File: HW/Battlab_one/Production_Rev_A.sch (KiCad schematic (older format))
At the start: 51 parts, among them IC2 MIC5225-5.0YM5-TR, J1 BANANA_CONN, J3 BANANA_CONN, P1 USB_C_Plug, T1 750315371

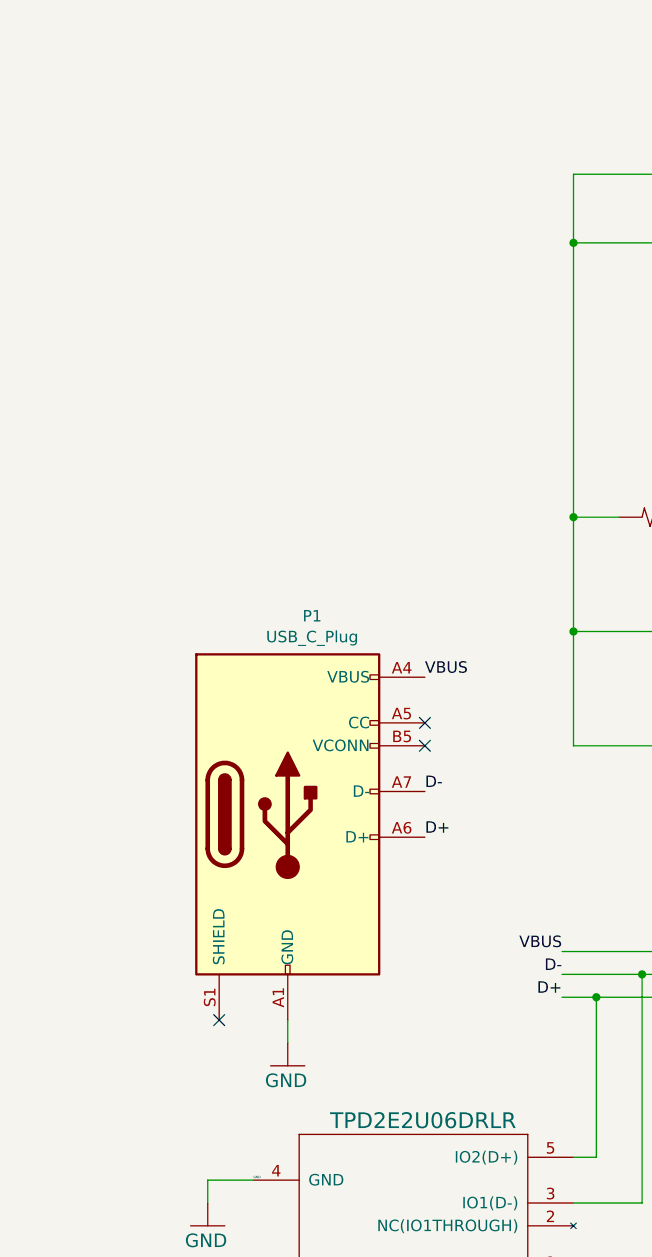
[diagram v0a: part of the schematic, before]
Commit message: USB-C resistor
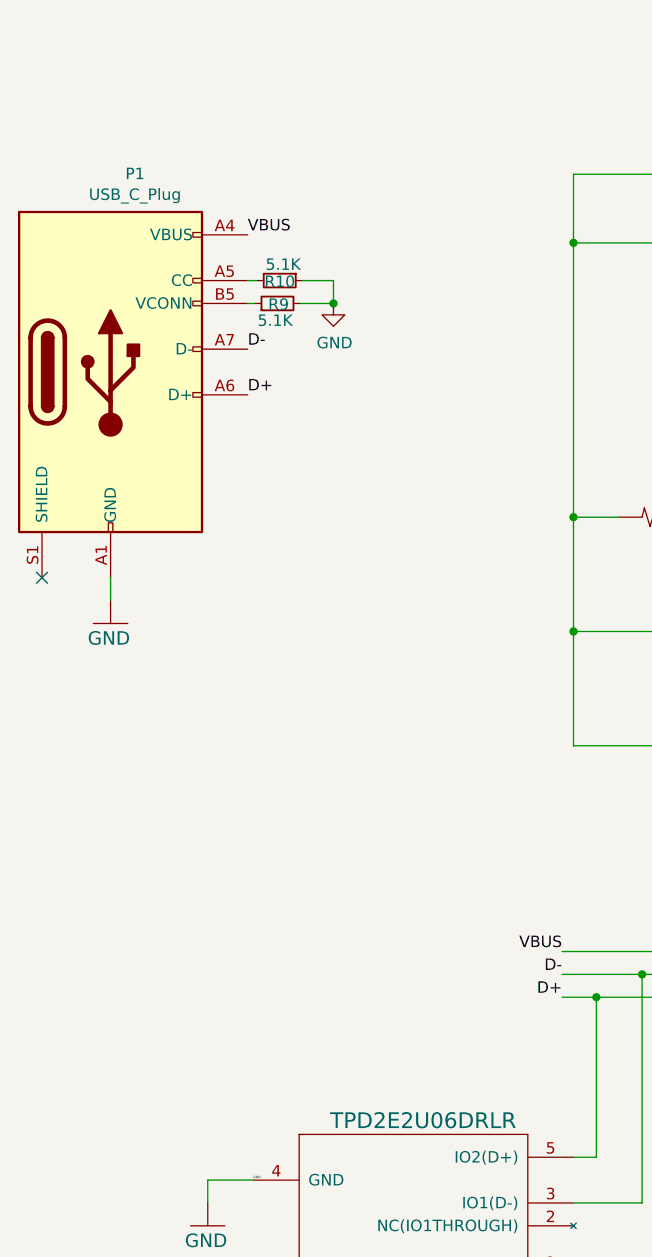
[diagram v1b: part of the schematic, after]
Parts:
- added R10, R9: 5.1K, Resistor_SMD:R_0805_2012Metric, symbol Device:R_Small
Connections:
- net GND: now also R10.1, R9.2
- net at P1.A5 (CC): now also R10.2
- net at P1.B5 (VCONN): now also R9.1
- no-connect marks 3 -> 1
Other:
- moved on the sheet: P1
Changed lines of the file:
@@
 Text Label 2650 5100 2    50   ~ 0
 D-
-NoConn ~ 1150 5300
-NoConn ~ 2050 4100
-NoConn ~ 2050 4000
+NoConn ~ 375  3365
 Wire Wire Line
-	1450 5300 1450 5400
+	675  3365 675  3465
 $Comp
 L Connector:USB_C_Plug_USB2.0 P1
 U 1 1 5F58B2D2
-P 1450 4400
-F 0 "P1" H 1557 5267 50  0000 C CNN
-F 1 "USB_C_Plug" H 1557 5176 50  0000 C CNN
-F 2 "Production_Rev_A:C393939" H 1600 4400 50  0001 C CNN
-F 3 "https://www.usb.org/sites/default/files/documents/usb_type-c.zip" H 1600 4400 50  0001 C CNN
-	1    1450 4400
+P 675 2465
+F 0 "P1" H 782 3332 50  0000 C CNN
+F 1 "USB_C_Plug" H 782 3241 50  0000 C CNN
+F 2 "Production_Rev_A:C393939" H 825 2465 50  0001 C CNN
+F 3 "https://www.usb.org/sites/default/files/documents/usb_type-c.zip" H 825 2465 50  0001 C CNN
+	1    675  2465
 	1    0    0    -1
 $EndComp
-Text Label 2050 3800 0    50   ~ 0
+Text Label 1275 1865 0    50   ~ 0
 VBUS
-Text Label 2050 4300 0    50   ~ 0
+Text Label 1275 2365 0    50   ~ 0
 D-
-Text Label 2050 4500 0    50   ~ 0
+Text Label 1275 2565 0    50   ~ 0
 D+
 $Comp
 L Production_Rev_A-eagle-import:GND #GND09
 U 1 1 928DF91D
-P 1450 5500
-F 0 "#GND09" H 1450 5500 50  0001 C CNN
-F 1 "GND" H 1350 5400 59  0000 L BNN
-F 2 "" H 1450 5500 50  0001 C CNN
-F 3 "" H 1450 5500 50  0001 C CNN
-	1    1450 5500
+P 675 3565
+F 0 "#GND09" H 675 3565 50  0001 C CNN
+F 1 "GND" H 575 3465 59  0000 L BNN
+F 2 "" H 675 3565 50  0001 C CNN
+F 3 "" H 675 3565 50  0001 C CNN
+	1    675  3565
 	1    0    0    -1
 $EndComp
 $Comp
-L Production_Rev_A-eagle-import:GND #GND?
+L Production_Rev_A-eagle-import:GND #GND06
 U 1 1 5FC299E3
 P 1100 6200
-F 0 "#GND?" H 1100 6200 50  0001 C CNN
+F 0 "#GND06" H 1100 6200 50  0001 C CNN
 F 1 "GND" H 1000 6100 59  0000 L BNN
 F 2 "" H 1100 6200 50  0001 C CNN
@@
 	1    0    0    -1
 $EndComp
+$Comp
+L Device:R_Small R10
+U 1 1 5F5C899C
+P 1415 2065
+F 0 "R10" V 1420 2065 50  0000 C CNN
+F 1 "5.1K" V 1345 2080 50  0000 C CNN
+F 2 "Resistor_SMD:R_0805_2012Metric" H 1415 2065 50  0001 C CNN
+F 3 "~" H 1415 2065 50  0001 C CNN
+	1    1415 2065
+	0    1    1    0
+$EndComp
+Wire Wire Line
+	1315 2065 1275 2065
+Wire Wire Line
+	1275 2165 1305 2165
+$Comp
+L Device:R_Small R9
+U 1 1 5F609895
+P 1405 2165
+F 0 "R9" V 1400 2160 50  0000 C CNN
+F 1 "5.1K" V 1330 2175 50  0000 C CNN
+F 2 "Resistor_SMD:R_0805_2012Metric" H 1405 2165 50  0001 C CNN
+F 3 "~" H 1405 2165 50  0001 C CNN
+	1    1405 2165
+	0    -1   -1   0
+$EndComp
+$Comp
+L power:GND #PWR01
+U 1 1 5F60B49F
+P 1650 2165
+F 0 "#PWR01" H 1650 1915 50  0001 C CNN
+F 1 "GND" H 1655 1992 50  0000 C CNN
+F 2 "" H 1650 2165 50  0001 C CNN
+F 3 "" H 1650 2165 50  0001 C CNN
+	1    1650 2165
+	1    0    0    -1
+$EndComp
+Wire Wire Line
+	1515 2065 1650 2065
+Wire Wire Line
+	1650 2065 1650 2165
+Wire Wire Line
+	1505 2165 1650 2165
+Connection ~ 1650 2165
 $EndSCHEMATC

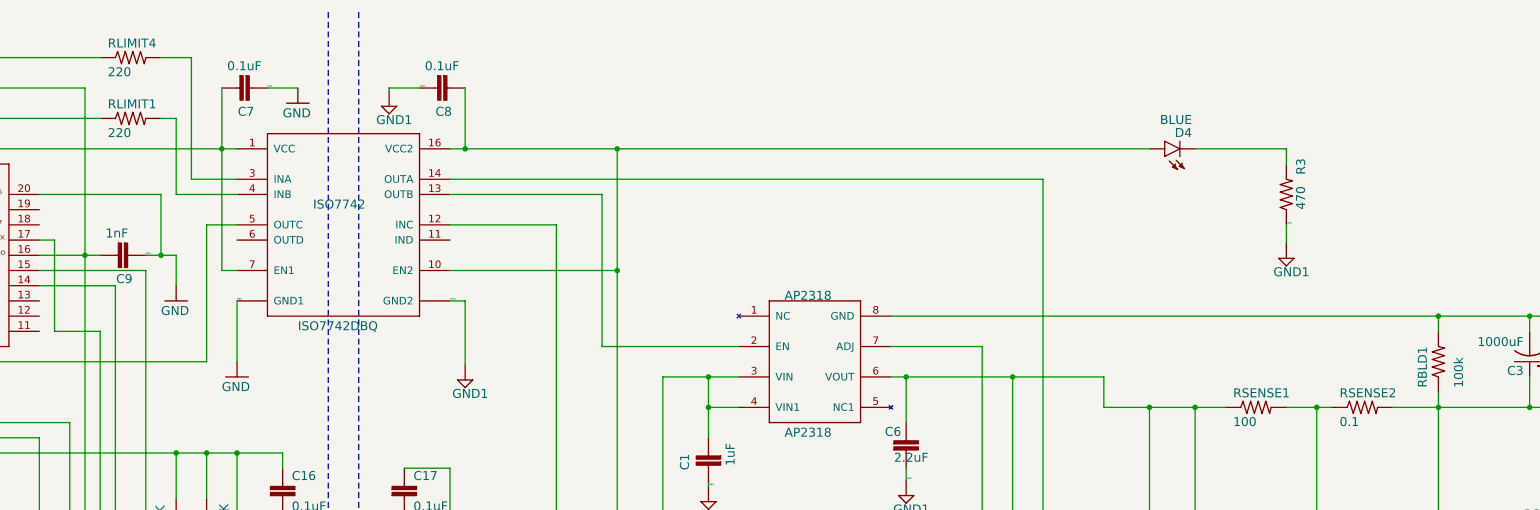
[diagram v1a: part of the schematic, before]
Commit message: Silkscreen moved
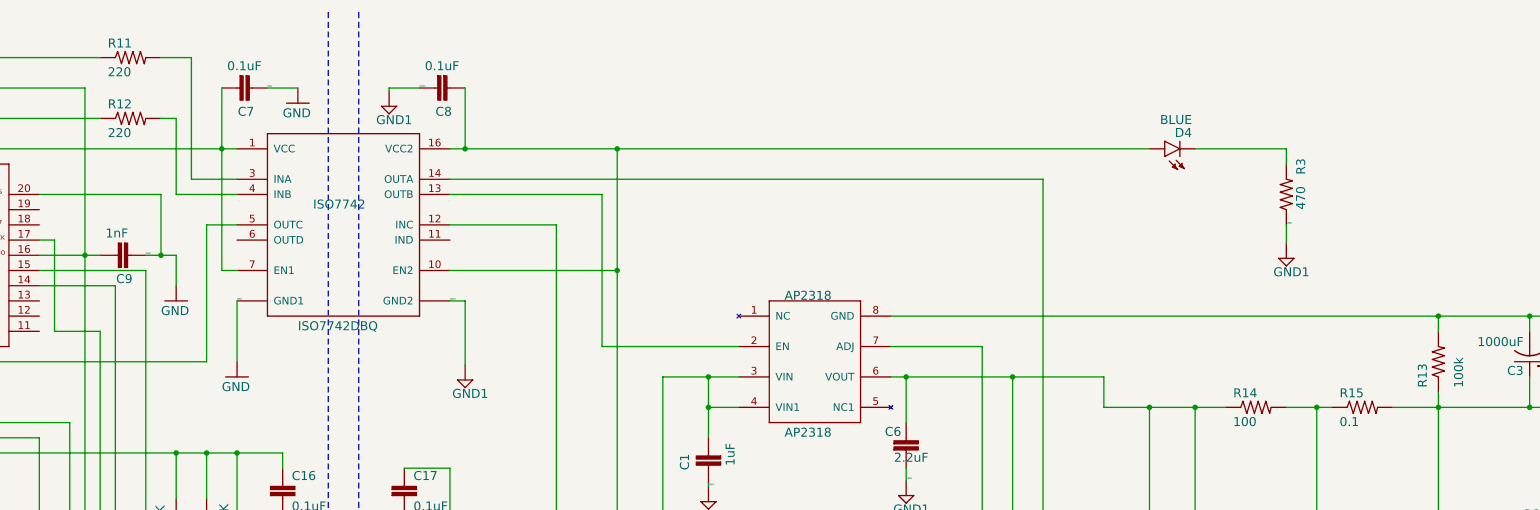
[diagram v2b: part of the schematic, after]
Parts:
- renumbered RLIMIT4 to R11, RLIMIT1 to R12, RBLD1 to R13, RSENSE1 to R14, RSENSE2 to R15
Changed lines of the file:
@@
 $EndComp
 $Comp
-L Production_Rev_A-eagle-import:RESISTOR1206 RSENSE2
+L Production_Rev_A-eagle-import:RESISTOR1206 R15
 U 1 1 3C099C55
 P 14600 3300
-F 0 "RSENSE2" H 14450 3359 59  0000 L BNN
+F 0 "R15" H 14450 3359 59  0000 L BNN
 F 1 "0.1" H 14450 3170 59  0000 L BNN
 F 2 "Production_Rev_A:1206" H 14600 3300 50  0001 C CNN
@@
 $EndComp
 $Comp
-L Production_Rev_A-eagle-import:RESISTOR1206 RLIMIT1
+L Production_Rev_A-eagle-import:RESISTOR1206 R12
 U 1 1 500A3A76
 P 6500 1400
-F 0 "RLIMIT1" H 6350 1459 59  0000 L BNN
+F 0 "R12" H 6350 1459 59  0000 L BNN
 F 1 "220" H 6350 1270 59  0000 L BNN
 F 2 "Production_Rev_A:1206" H 6500 1400 50  0001 C CNN
@@
 $EndComp
 $Comp
-L Production_Rev_A-eagle-import:RESISTOR1206 RSENSE1
+L Production_Rev_A-eagle-import:RESISTOR1206 R14
 U 1 1 B4C89A37
 P 13900 3300
-F 0 "RSENSE1" H 13750 3359 59  0000 L BNN
+F 0 "R14" H 13750 3359 59  0000 L BNN
 F 1 "100" H 13750 3170 59  0000 L BNN
 F 2 "Production_Rev_A:1206" H 13900 3300 50  0001 C CNN
@@
 $EndComp
 $Comp
-L Production_Rev_A-eagle-import:RESISTOR1206 RLIMIT4
+L Production_Rev_A-eagle-import:RESISTOR1206 R11
 U 1 1 46625473
 P 6500 1000
-F 0 "RLIMIT4" H 6350 1059 59  0000 L BNN
+F 0 "R11" H 6350 1059 59  0000 L BNN
 F 1 "220" H 6350 870 59  0000 L BNN
 F 2 "Production_Rev_A:1206" H 6500 1000 50  0001 C CNN
@@
 $EndComp
 $Comp
-L Production_Rev_A-eagle-import:RESISTOR1206 RBLD1
+L Production_Rev_A-eagle-import:RESISTOR1206 R13
 U 1 1 983D86E5
 P 15100 3000
-F 0 "RBLD1" H 14930 3069 59  0000 L BNN
+F 0 "R13" H 14930 3069 59  0000 L BNN
 F 1 "100k" H 15130 2900 59  0000 R TNN
 F 2 "Production_Rev_A:1206" H 15100 3000 50  0001 C CNN

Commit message: manf#
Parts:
- AD5248: manf# (none) -> 584-AD5248BRMZ100
- AP2318: manf# (none) -> 621-AP2318M-ADJTRG1
- FTDI232RL1: manf# (none) -> C8690
- IC2: manf# (none) -> C145704
- INA233: manf# (none) -> 595-INA233AIDGST
- ISO1540: manf# (none) -> C179739
- ISO7742: manf# (none) -> 595-ISO7742DBQ
- MSP430: manf# (none) -> C107631
- SN6505: manf# (none) -> C74518
- T1: manf# (none) -> 710-750315371
- USBPROT1: manf# (none) -> 595-TPD2E2U06DRLR
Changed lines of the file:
@@
 	5400 8100 5800 8100
-Wire Wire Line
-	5800 8100 5800 8900
-Wire Wire Line
-	5800 8900 3800 8900
 Wire Wire Line
 	3800 8900 3800 8100
@@
 F 2 "Production_Rev_A:SSOP28DB" H 4900 5100 50  0001 C CNN
 F 3 "" H 4900 5100 50  0001 C CNN
+F 4 "C8690" H 4900 5100 50  0001 C CNN "manf#"
 	1    4900 5100
 	1    0    0    -1
@@
 F 2 "Production_Rev_A:SOIC-8" H 11000 3000 50  0001 C CNN
 F 3 "" H 11000 3000 50  0001 C CNN
+F 4 "621-AP2318M-ADJTRG1" H 11000 3000 50  0001 C CNN "manf#"
 	1    11000 3000
 	1    0    0    -1
@@
 F 2 "Production_Rev_A:VSSOP-10" H 11100 7300 50  0001 C CNN
 F 3 "" H 11100 7300 50  0001 C CNN
+F 4 "595-INA233AIDGST" H 11100 7300 50  0001 C CNN "manf#"
 	1    11100 7300
 	1    0    0    -1
@@
 F 2 "Production_Rev_A:MSOP-10" H 11000 5200 50  0001 C CNN
 F 3 "" H 11000 5200 50  0001 C CNN
+F 4 "584-AD5248BRMZ100" H 11000 5200 50  0001 C CNN "manf#"
 	1    11000 5200
 	1    0    0    -1
@@
 F 2 "Production_Rev_A:PW20" H 5000 2300 50  0001 C CNN
 F 3 "" H 5000 2300 50  0001 C CNN
+F 4 "C107631" H 5000 2300 50  0001 C CNN "manf#"
 	1    5000 2300
 	1    0    0    -1
@@
 F 2 "Production_Rev_A:TOR-6P-HT4_SMT_6PIN_(1201)" H 7900 7400 50  0001 C CNN
 F 3 "" H 7900 7400 50  0001 C CNN
+F 4 "710-750315371" H 7900 7400 50  0001 C CNN "manf#"
 	1    7900 7400
-	1    0    0    -1
-$EndComp
-$Comp
-L Production_Rev_A-eagle-import:SN6505 SN6505
-U 1 1 5779FEE2
-P 5400 8500
-F 0 "SN6505" H 4700 9500 42  0000 L BNN
-F 1 "SN6505" H 4700 8200 42  0000 L BNN
-F 2 "Production_Rev_A:SOT95P280X145-6N" H 5400 8500 50  0001 C CNN
-F 3 "" H 5400 8500 50  0001 C CNN
-	1    5400 8500
 	1    0    0    -1
 $EndComp
@@
 F 2 "Production_Rev_A:SOIC127P600X175-8N" H 9100 5600 50  0001 C CNN
 F 3 "" H 9100 5600 50  0001 C CNN
+F 4 "C179739" H 9100 5600 50  0001 C CNN "manf#"
 	1    9100 5600
 	1    0    0    -1
@@
 F 2 "Production_Rev_A:SOP63P599X175-16N" H 7900 2100 50  0001 C CNN
 F 3 "" H 7900 2100 50  0001 C CNN
+F 4 "595-ISO7742DBQ" H 7900 2100 50  0001 C CNN "manf#"
 	1    7900 2100
 	1    0    0    -1
@@
 F 2 "Production_Rev_A:SOT50P160X60-5N" H 2000 6300 50  0001 C CNN
 F 3 "" H 2000 6300 50  0001 C CNN
+F 4 "595-TPD2E2U06DRLR" H 2000 6300 50  0001 C CNN "manf#"
 	1    2000 6300
 	-1   0    0    1
@@
 F 2 "Production_Rev_A:SOT95P280X130-5N" H 10400 8700 50  0001 C CNN
 F 3 "" H 10400 8700 50  0001 C CNN
+F 4 "C145704" H 10400 8700 50  0001 C CNN "manf#"
 	1    10400 8700
 	1    0    0    -1
@@
 	1505 2165 1650 2165
 Connection ~ 1650 2165
+Wire Wire Line
+	5800 8900 3800 8900
+Wire Wire Line
+	5800 8100 5800 8900
+$Comp
+L Production_Rev_A-eagle-import:SN6505 SN6505
+U 1 1 5779FEE2
+P 5400 8500
+F 0 "SN6505" H 4700 9500 42  0000 L BNN
+F 1 "SN6505" H 4700 8200 42  0000 L BNN
+F 2 "Production_Rev_A:SOT95P280X145-6N" H 5400 8500 50  0001 C CNN
+F 3 "" H 5400 8500 50  0001 C CNN
+F 4 "C74518" H 5400 8500 50  0001 C CNN "manf#"
+	1    5400 8500
+	1    0    0    -1
+$EndComp
 $EndSCHEMATC

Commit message: manf#
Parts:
- C1, C10, C4: manf# (none) -> C123655
- C11, C14, C16, C17, C5, C7, C8: manf# (none) -> C110253
- C12, C13: manf# (none) -> C513774
- C15, C2, C6: manf# (none) -> C141195
- C3: manf# (none) -> C249843
- C9: manf# (none) -> C1845
- D2, D3: manf# (none) -> 863-MBR0520LT1G
- D4: manf# (none) -> C375460
- J1, J3: manf# (none) -> C106273
- P-MOS1: manf# (none) -> C518789
- P1: manf# (none) -> C393939
- R1, R2, R6, R7: manf# (none) -> C104602
- R10, R9: manf# (none) -> C164004
- R11, R12: manf# (none) -> C137353
- R13: manf# (none) -> C702843
- R14, R8: manf# (none) -> C723762
- R15: manf# (none) -> C149672
- R3: manf# (none) -> C104814
- R4, R5: manf# (none) -> C429214
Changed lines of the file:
@@
 F 2 "Production_Rev_A:1206" H 6800 4100 50  0001 C CNN
 F 3 "" H 6800 4100 50  0001 C CNN
+F 4 "C104602" H 6800 4100 50  0001 C CNN "manf#"
 	1    6800 4100
 	0    -1   -1   0
@@
 F 2 "Production_Rev_A:1206" H 7000 4100 50  0001 C CNN
 F 3 "" H 7000 4100 50  0001 C CNN
+F 4 "C104602" H 7000 4100 50  0001 C CNN "manf#"
 	1    7000 4100
 	0    -1   -1   0
@@
 F 2 "Production_Rev_A:1206" H 12300 5400 50  0001 C CNN
 F 3 "" H 12300 5400 50  0001 C CNN
+F 4 "C141195" H 12300 5400 50  0001 C CNN "manf#"
 	1    12300 5400
 	1    0    0    -1
@@
 F 2 "Production_Rev_A:1206" H 14600 3300 50  0001 C CNN
 F 3 "" H 14600 3300 50  0001 C CNN
+F 4 "C149672" H 14600 3300 50  0001 C CNN "manf#"
 	1    14600 3300
 	1    0    0    -1
@@
 F 2 "Production_Rev_A:1206" H 10300 3600 50  0001 C CNN
 F 3 "" H 10300 3600 50  0001 C CNN
+F 4 "C123655" H 10300 3600 50  0001 C CNN "manf#"
 	1    10300 3600
 	-1   0    0    1
@@
 F 2 "Production_Rev_A:PANASONIC_F" H 15700 3000 50  0001 C CNN
 F 3 "" H 15700 3000 50  0001 C CNN
+F 4 "C249843" H 15700 3000 50  0001 C CNN "manf#"
 	1    15700 3000
 	-1   0    0    1
@@
 F 2 "Production_Rev_A:1206" H 4100 3100 50  0001 C CNN
 F 3 "" H 4100 3100 50  0001 C CNN
+F 4 "C110253" H 4100 3100 50  0001 C CNN "manf#"
 	1    4100 3100
 	0    1    1    0
@@
 F 2 "Production_Rev_A:1206" H 4800 1200 50  0001 C CNN
 F 3 "" H 4800 1200 50  0001 C CNN
+F 4 "C429214" H 4800 1200 50  0001 C CNN "manf#"
 	1    4800 1200
 	1    0    0    -1
@@
 F 2 "Production_Rev_A:1206" H 6400 2300 50  0001 C CNN
 F 3 "" H 6400 2300 50  0001 C CNN
+F 4 "C1845" H 6400 2300 50  0001 C CNN "manf#"
 	1    6400 2300
 	0    1    1    0
@@
 F 2 "Production_Rev_A:1206" H 3100 3100 50  0001 C CNN
 F 3 "" H 3100 3100 50  0001 C CNN
+F 4 "C429214" H 3100 3100 50  0001 C CNN "manf#"
 	1    3100 3100
 	-1   0    0    1
@@
 F 2 "Production_Rev_A:1206" H 6500 1400 50  0001 C CNN
 F 3 "" H 6500 1400 50  0001 C CNN
+F 4 "C137353" H 6500 1400 50  0001 C CNN "manf#"
 	1    6500 1400
 	1    0    0    -1
@@
 F 2 "Production_Rev_A:1206" H 16000 3010 50  0001 C CNN
 F 3 "" H 16000 3010 50  0001 C CNN
+F 4 "C110253" H 16000 3010 50  0001 C CNN "manf#"
 	1    16000 3010
 	1    0    0    -1
@@
 F 2 "Production_Rev_A:1206" H 3800 9300 50  0001 C CNN
 F 3 "" H 3800 9300 50  0001 C CNN
+F 4 "C513774" H 3800 9300 50  0001 C CNN "manf#"
 	1    3800 9300
 	1    0    0    -1
@@
 F 2 "Production_Rev_A:SOD3716X117(SOD-123)" H 8800 7100 50  0001 C CNN
 F 3 "" H 8800 7100 50  0001 C CNN
+F 4 "863-MBR0520LT1G" H 8800 7100 50  0001 C CNN "manf#"
 	1    8800 7100
 	1    0    0    -1
@@
 F 2 "Production_Rev_A:SOD3716X117(SOD-123)" H 8900 7700 50  0001 C CNN
 F 3 "" H 8900 7700 50  0001 C CNN
+F 4 "863-MBR0520LT1G" H 8900 7700 50  0001 C CNN "manf#"
 	1    8900 7700
 	1    0    0    -1
@@
 F 2 "Production_Rev_A:1206" H 9300 8100 50  0001 C CNN
 F 3 "" H 9300 8100 50  0001 C CNN
+F 4 "C513774" H 9300 8100 50  0001 C CNN "manf#"
 	1    9300 8100
 	1    0    0    -1
@@
 F 2 "Production_Rev_A:1206" H 9800 8100 50  0001 C CNN
 F 3 "" H 9800 8100 50  0001 C CNN
+F 4 "C110253" H 9800 8100 50  0001 C CNN "manf#"
 	1    9800 8100
 	1    0    0    -1
@@
 F 2 "Production_Rev_A:1206" H 8800 4600 50  0001 C CNN
 F 3 "" H 8800 4600 50  0001 C CNN
+F 4 "C104602" H 8800 4600 50  0001 C CNN "manf#"
 	1    8800 4600
 	0    1    1    0
@@
 F 2 "Production_Rev_A:1206" H 9100 4600 50  0001 C CNN
 F 3 "" H 9100 4600 50  0001 C CNN
+F 4 "C104602" H 9100 4600 50  0001 C CNN "manf#"
 	1    9100 4600
 	0    1    1    0
@@
 F 2 "Production_Rev_A:1206" H 3300 2200 50  0001 C CNN
 F 3 "" H 3300 2200 50  0001 C CNN
+F 4 "C123655" H 3300 2200 50  0001 C CNN "manf#"
 	1    3300 2200
 	-1   0    0    1
@@
 F 2 "Production_Rev_A:1206" H 13900 3300 50  0001 C CNN
 F 3 "" H 13900 3300 50  0001 C CNN
+F 4 "C723762" H 13900 3300 50  0001 C CNN "manf#"
 	1    13900 3300
 	1    0    0    -1
@@
 F 2 "Production_Rev_A:SOT23-3" H 13800 4400 50  0001 C CNN
 F 3 "" H 13800 4400 50  0001 C CNN
+F 4 "C518789" H 13800 4400 50  0001 C CNN "manf#"
 	1    13800 4400
 	0    -1   -1   0
@@
 F 2 "Production_Rev_A:1206" H 6500 1000 50  0001 C CNN
 F 3 "" H 6500 1000 50  0001 C CNN
+F 4 "C137353" H 6500 1000 50  0001 C CNN "manf#"
 	1    6500 1000
 	1    0    0    -1
@@
 F 2 "Production_Rev_A:1206" H 15900 4100 50  0001 C CNN
 F 3 "" H 15900 4100 50  0001 C CNN
+F 4 "C723762" H 15900 4100 50  0001 C CNN "manf#"
 	1    15900 4100
 	-1   0    0    1
@@
 F 2 "Production_Rev_A:1206" H 11600 3600 50  0001 C CNN
 F 3 "" H 11600 3600 50  0001 C CNN
+F 4 "C141195" H 11600 3600 50  0001 C CNN "manf#"
 	1    11600 3600
 	1    0    0    -1
@@
 F 2 "Production_Rev_A:1206" H 7200 1200 50  0001 C CNN
 F 3 "" H 7200 1200 50  0001 C CNN
+F 4 "C110253" H 7200 1200 50  0001 C CNN "manf#"
 	1    7200 1200
 	0    1    1    0
@@
 F 2 "Production_Rev_A:1206" H 8500 1200 50  0001 C CNN
 F 3 "" H 8500 1200 50  0001 C CNN
+F 4 "C110253" H 8500 1200 50  0001 C CNN "manf#"
 	1    8500 1200
 	0    1    1    0
@@
 F 2 "Production_Rev_A:LED-1206" H 13300 1600 50  0001 C CNN
 F 3 "" H 13300 1600 50  0001 C CNN
+F 4 "C375460" H 13300 1600 50  0001 C CNN "manf#"
 	1    13300 1600
 	0    -1   -1   0
@@
 F 2 "Production_Rev_A:1206" H 14100 1900 50  0001 C CNN
 F 3 "" H 14100 1900 50  0001 C CNN
+F 4 "C104814" H 14100 1900 50  0001 C CNN "manf#"
 	1    14100 1900
 	0    -1   -1   0
@@
 F 2 "Production_Rev_A:1206" H 10000 9150 50  0001 C CNN
 F 3 "" H 10000 9150 50  0001 C CNN
+F 4 "C123655" H 10000 9150 50  0001 C CNN "manf#"
 	1    10000 9150
 	1    0    0    -1
@@
 F 2 "Production_Rev_A:1206" H 11800 9290 50  0001 C CNN
 F 3 "" H 11800 9290 50  0001 C CNN
+F 4 "C141195" H 11800 9290 50  0001 C CNN "manf#"
 	1    11800 9290
 	1    0    0    -1
@@
 F 2 "Production_Rev_A:1206" H 7500 3900 50  0001 C CNN
 F 3 "" H 7500 3900 50  0001 C CNN
+F 4 "C110253" H 7500 3900 50  0001 C CNN "manf#"
 	1    7500 3900
 	1    0    0    -1
@@
 F 2 "Production_Rev_A:1206" H 8300 3900 50  0001 C CNN
 F 3 "" H 8300 3900 50  0001 C CNN
+F 4 "C110253" H 8300 3900 50  0001 C CNN "manf#"
 	1    8300 3900
 	1    0    0    -1
@@
 F 2 "Production_Rev_A:BANANA_CONN" H 16700 3300 50  0001 C CNN
 F 3 "" H 16700 3300 50  0001 C CNN
+F 4 "C106273" H 16700 3300 50  0001 C CNN "manf#"
 	1    16700 3300
 	1    0    0    -1
@@
 F 2 "Production_Rev_A:BANANA_CONN" H 16700 2700 50  0001 C CNN
 F 3 "" H 16700 2700 50  0001 C CNN
+F 4 "C106273" H 16700 2700 50  0001 C CNN "manf#"
 	1    16700 2700
 	1    0    0    -1
@@
 F 2 "Production_Rev_A:1206" H 15100 3000 50  0001 C CNN
 F 3 "" H 15100 3000 50  0001 C CNN
+F 4 "C702843" H 15100 3000 50  0001 C CNN "manf#"
 	1    15100 3000
 	0    -1   -1   0
@@
 F 2 "Production_Rev_A:C393939" H 825 2465 50  0001 C CNN
 F 3 "https://www.usb.org/sites/default/files/documents/usb_type-c.zip" H 825 2465 50  0001 C CNN
+F 4 "C393939" H 675 2465 50  0001 C CNN "manf#"
 	1    675  2465
 	1    0    0    -1
@@
 F 2 "Resistor_SMD:R_0805_2012Metric" H 1415 2065 50  0001 C CNN
 F 3 "~" H 1415 2065 50  0001 C CNN
+F 4 "C164004" H 1415 2065 50  0001 C CNN "manf#"
 	1    1415 2065
 	0    1    1    0
@@
 F 2 "Resistor_SMD:R_0805_2012Metric" H 1405 2165 50  0001 C CNN
 F 3 "~" H 1405 2165 50  0001 C CNN
+F 4 "C164004" H 1405 2165 50  0001 C CNN "manf#"
 	1    1405 2165
 	0    -1   -1   0
